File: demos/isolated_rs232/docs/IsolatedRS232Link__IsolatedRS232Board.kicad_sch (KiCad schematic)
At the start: 9 parts, among them J1 Header1xNFemale, J2 Header1xNFemale

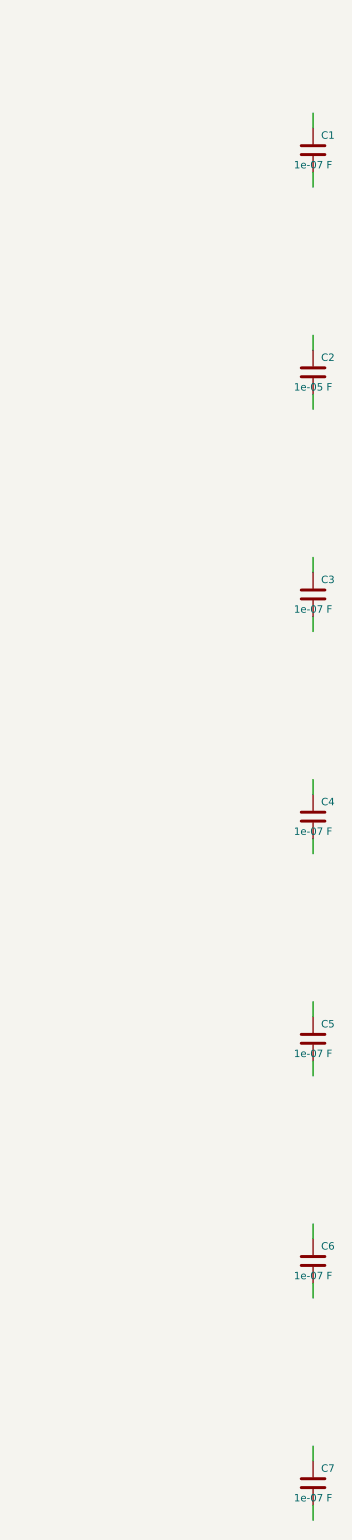
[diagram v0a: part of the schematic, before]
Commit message: framework: passive + diode terminals mandatory (#30)
Continuation of the LED.cathode regression fix (#29). Resistor,
Capacitor, Inductor, and every Diode subclass had their terminals
declared `mandatory=False` with the same "structurally inert under
graph evaluation" justification — letting demos declare BOM-only
timing / decoupling / pull-up parts without wiring them, then ship
breadboard SVGs and netlists where those parts sat orphaned.

A real resistor / capacitor / inductor / diode with a dangling
terminal does nothing. Marking the ports mandatory closes the
silent regression at the framework layer.

  - `src/components/passives/{resistor,capacitor,inductor}.py` and
    every diode subclass under `src/components/diodes/` now declare
    their terminals `mandatory=True`.
  - `tests/components/test_{resistor,capacitor,inductor}.py`:
    regression tests pin the new contract per component.
  - `tests/components/test_diode_mandatory_terminals.py` (new):
    parametrized over D1N4001 / D1N4007 / D1N4148 / D1N4728A /
    D1N4733A / D1N4742A / D1N5817.
  - Six demos (`backup_power`, `bldc_motor`, `dice`,
    `doorbell_protector`, `fan_cooling`, `isolated_rs232`) had
    declared-but-unwired passives — each now wires them either to
    their datasheet-correct net (e.g. DoorbellProtector's flyback
    diode anode joins the relay coil_minus net) or as an isolated
    0-Ω passthrough with `dynamically_driven=True` where the part
    is genuinely BOM-only and the voltage-only simulator can't
    honour its behaviour. Comments at each call site explain
    which kind.
  - Test fixtures across CLI, refdes, format-roundtrip, kicad
    import, and per-format renderer tests updated so they still
    pin down the specific error each one exists to catch without
    tripping the new mandatory-pin check first.
  - All demo docs regenerated; goldens refreshed.

After this commit the breadboard SVGs show every BOM part connected
to something — no more orphaned caps and resistors float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
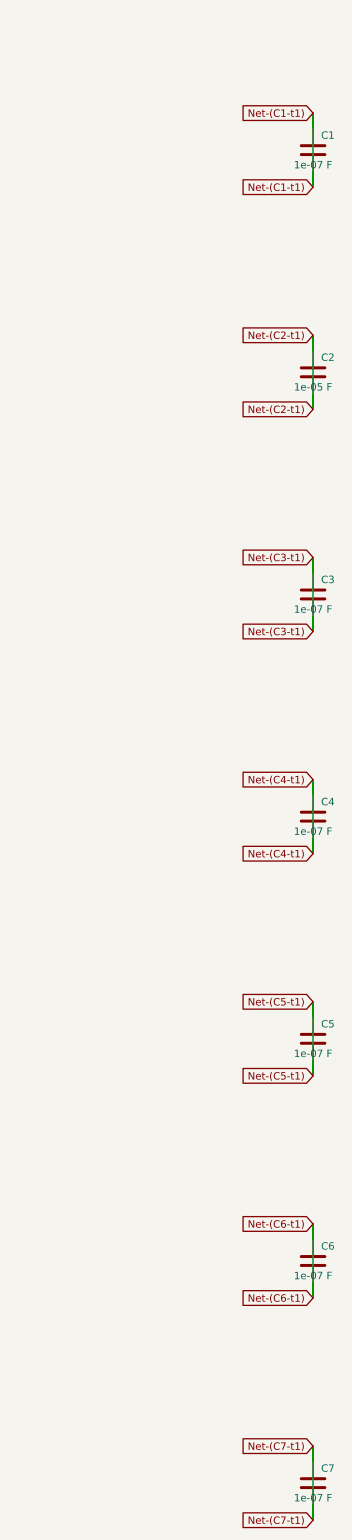
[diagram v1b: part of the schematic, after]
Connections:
- net Net-(C2-t1): now reaches C2.1
- net Net-(C2-t1): now also C2.2
- net Net-(C7-t1): now reaches C7.1
- net Net-(C7-t1): now also C7.2
- net Net-(C3-t1): now reaches C3.1
- net Net-(C3-t1): now also C3.2
- net Net-(C4-t1): now reaches C4.1
- net Net-(C4-t1): now also C4.2
- net Net-(C1-t1): now reaches C1.1
- net Net-(C1-t1): now also C1.2
- net Net-(C5-t1): now reaches C5.1
- net Net-(C5-t1): now also C5.2
- net Net-(C6-t1): now reaches C6.1
- net Net-(C6-t1): now also C6.2
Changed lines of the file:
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@@
     (stroke (width 0) (type default))
+  )
+  (global_label "Net-(C1-t1)"
+    (shape input)
+    (at 63.5 184.15 0)
+    (fields_autoplaced yes)
+    (effects (font (size 1.27 1.27)) (justify right))
+    (property "Intersheet References" "${INTERSHEET_REFS}"
+      (at 0 0 0)
+      (effects (font (size 1.27 1.27)) (hide yes))
+    )
   )
   (wire
     (pts (xy 63.5 173.99) (xy 63.5 171.45))
     (stroke (width 0) (type default))
+  )
+  (global_label "Net-(C1-t1)"
+    (shape input)
+    (at 63.5 171.45 0)
+    (fields_autoplaced yes)
+    (effects (font (size 1.27 1.27)) (justify right))
+    (property "Intersheet References" "${INTERSHEET_REFS}"
+      (at 0 0 0)
+      (effects (font (size 1.27 1.27)) (hide yes))
+    )
   )
   (symbol
@@
     (stroke (width 0) (type default))
   )
+  (global_label "Net-(C2-t1)"
+    (shape input)
+    (at 63.5 222.25 0)
+    (fields_autoplaced yes)
+    (effects (font (size 1.27 1.27)) (justify right))
+    (property "Intersheet References" "${INTERSHEET_REFS}"
+      (at 0 0 0)
+      (effects (font (size 1.27 1.27)) (hide yes))
+    )
+  )
   (wire
     (pts (xy 63.5 212.09) (xy 63.5 209.55))
     (stroke (width 0) (type default))
+  )
+  (global_label "Net-(C2-t1)"
+    (shape input)
+    (at 63.5 209.55 0)
+    (fields_autoplaced yes)
+    (effects (font (size 1.27 1.27)) (justify right))
+    (property "Intersheet References" "${INTERSHEET_REFS}"
+      (at 0 0 0)
+      (effects (font (size 1.27 1.27)) (hide yes))
+    )
   )
   (symbol
@@
     (stroke (width 0) (type default))
   )
+  (global_label "Net-(C3-t1)"
+    (shape input)
+    (at 63.5 260.35 0)
+    (fields_autoplaced yes)
+    (effects (font (size 1.27 1.27)) (justify right))
+    (property "Intersheet References" "${INTERSHEET_REFS}"
+      (at 0 0 0)
+      (effects (font (size 1.27 1.27)) (hide yes))
+    )
+  )
   (wire
     (pts (xy 63.5 250.19) (xy 63.5 247.65))
     (stroke (width 0) (type default))
+  )
+  (global_label "Net-(C3-t1)"
+    (shape input)
+    (at 63.5 247.65 0)
+    (fields_autoplaced yes)
+    (effects (font (size 1.27 1.27)) (justify right))
+    (property "Intersheet References" "${INTERSHEET_REFS}"
+      (at 0 0 0)
+      (effects (font (size 1.27 1.27)) (hide yes))
+    )
   )
   (symbol
@@
     (stroke (width 0) (type default))
   )
+  (global_label "Net-(C4-t1)"
+    (shape input)
+    (at 63.5 298.45 0)
+    (fields_autoplaced yes)
+    (effects (font (size 1.27 1.27)) (justify right))
+    (property "Intersheet References" "${INTERSHEET_REFS}"
+      (at 0 0 0)
+      (effects (font (size 1.27 1.27)) (hide yes))
+    )
+  )
   (wire
     (pts (xy 63.5 288.29) (xy 63.5 285.75))
     (stroke (width 0) (type default))
+  )
+  (global_label "Net-(C4-t1)"
+    (shape input)
+    (at 63.5 285.75 0)
+    (fields_autoplaced yes)
+    (effects (font (size 1.27 1.27)) (justify right))
+    (property "Intersheet References" "${INTERSHEET_REFS}"
+      (at 0 0 0)
+      (effects (font (size 1.27 1.27)) (hide yes))
+    )
   )
   (symbol
@@
     (stroke (width 0) (type default))
   )
+  (global_label "Net-(C5-t1)"
+    (shape input)
+    (at 63.5 336.55 0)
+    (fields_autoplaced yes)
+    (effects (font (size 1.27 1.27)) (justify right))
+    (property "Intersheet References" "${INTERSHEET_REFS}"
+      (at 0 0 0)
+      (effects (font (size 1.27 1.27)) (hide yes))
+    )
+  )
   (wire
     (pts (xy 63.5 326.39) (xy 63.5 323.85))
     (stroke (width 0) (type default))
+  )
+  (global_label "Net-(C5-t1)"
+    (shape input)
+    (at 63.5 323.85 0)
+    (fields_autoplaced yes)
+    (effects (font (size 1.27 1.27)) (justify right))
+    (property "Intersheet References" "${INTERSHEET_REFS}"
+      (at 0 0 0)
+      (effects (font (size 1.27 1.27)) (hide yes))
+    )
   )
   (symbol
@@
     (stroke (width 0) (type default))
   )
+  (global_label "Net-(C6-t1)"
+    (shape input)
+    (at 63.5 374.65 0)
+    (fields_autoplaced yes)
+    (effects (font (size 1.27 1.27)) (justify right))
+    (property "Intersheet References" "${INTERSHEET_REFS}"
+      (at 0 0 0)
+      (effects (font (size 1.27 1.27)) (hide yes))
+    )
+  )
   (wire
     (pts (xy 63.5 364.49) (xy 63.5 361.95))
     (stroke (width 0) (type default))
+  )
+  (global_label "Net-(C6-t1)"
+    (shape input)
+    (at 63.5 361.95 0)
+    (fields_autoplaced yes)
+    (effects (font (size 1.27 1.27)) (justify right))
+    (property "Intersheet References" "${INTERSHEET_REFS}"
+      (at 0 0 0)
+      (effects (font (size 1.27 1.27)) (hide yes))
+    )
   )
   (symbol
@@
     (stroke (width 0) (type default))
   )
+  (global_label "Net-(C7-t1)"
+    (shape input)
+    (at 63.5 412.75 0)
+    (fields_autoplaced yes)
+    (effects (font (size 1.27 1.27)) (justify right))
+    (property "Intersheet References" "${INTERSHEET_REFS}"
+      (at 0 0 0)
+      (effects (font (size 1.27 1.27)) (hide yes))
+    )
+  )
   (wire
     (pts (xy 63.5 402.59) (xy 63.5 400.05))
     (stroke (width 0) (type default))
+  )
+  (global_label "Net-(C7-t1)"
+    (shape input)
+    (at 63.5 400.05 0)
+    (fields_autoplaced yes)
+    (effects (font (size 1.27 1.27)) (justify right))
+    (property "Intersheet References" "${INTERSHEET_REFS}"
+      (at 0 0 0)
+      (effects (font (size 1.27 1.27)) (hide yes))
+    )
   )
   (symbol
@@
     (stroke (width 0) (type default))
   )
+  (wire
+    (pts (xy 63.5 171.45) (xy 63.5 184.15))
+    (stroke (width 0) (type default))
+  )
+  (wire
+    (pts (xy 63.5 209.55) (xy 63.5 222.25))
+    (stroke (width 0) (type default))
+  )
+  (wire
+    (pts (xy 63.5 247.65) (xy 63.5 260.35))
+    (stroke (width 0) (type default))
+  )
+  (wire
+    (pts (xy 63.5 285.75) (xy 63.5 298.45))
+    (stroke (width 0) (type default))
+  )
+  (wire
+    (pts (xy 63.5 323.85) (xy 63.5 336.55))
+    (stroke (width 0) (type default))
+  )
+  (wire
+    (pts (xy 63.5 361.95) (xy 63.5 374.65))
+    (stroke (width 0) (type default))
+  )
+  (wire
+    (pts (xy 63.5 400.05) (xy 63.5 412.75))
+    (stroke (width 0) (type default))
+  )

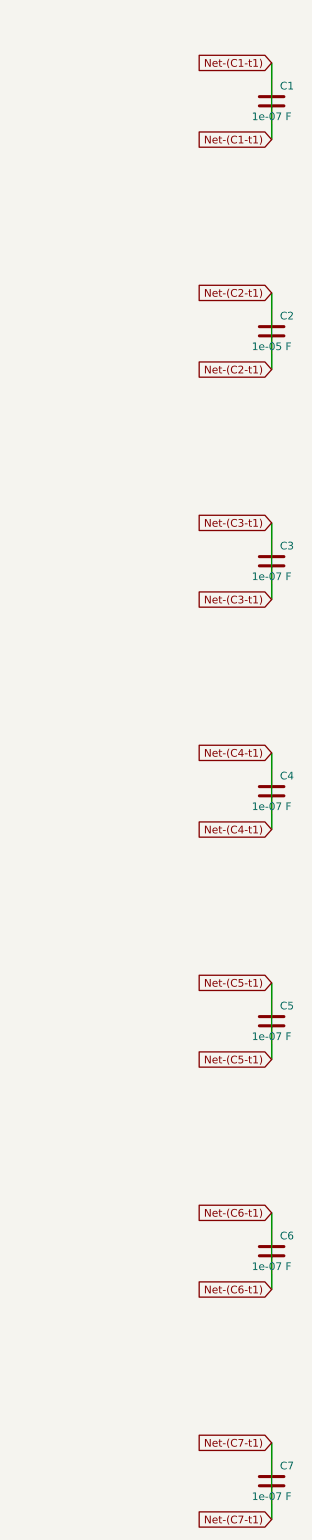
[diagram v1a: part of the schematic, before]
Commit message: units: Ohms.__str__ uses engineering notation (kΩ, MΩ, GΩ) (#33)
* units: Ohms.__str__ uses engineering notation (kΩ, MΩ, GΩ)

The previous `Ohms.__str__` formatted with bare `:.3g`, producing
unreadable scientific output for clean kilo / mega multiples:

  str(Ohms(10_000))     == "1e+04 Ω"      → now "10 kΩ"
  str(Ohms(100_000))    == "1e+05 Ω"      → now "100 kΩ"
  str(Ohms(1_000_000))  == "1e+06 Ω"      → now "1 MΩ"

The breadboard SVG visualiser surfaced the problem: a resistor body
labelled "100000Ω" makes a reader count zeros, while a label of
"100 kΩ" reads at a glance — exactly the convention every schematic
and parts catalogue uses. Centralising the engineering notation in
`Ohms.__str__` means every downstream consumer (assembly guide,
breadboard SVG, kicad netlist, BOM, reports) inherits the readable
form without each format adapter rolling its own formatter.

  - `Ohms.__str__` returns "47 Ω", "4.7 kΩ", "10 kΩ", "100 kΩ",
    "1 MΩ", "10 MΩ", "1 GΩ" per the kilo / mega / giga thresholds.
  - `Resistor.__str__` delegates to `str(self._ohms)` so it
    inherits the new notation (was producing the noisy "47.0 Ω"
    via raw float).
  - The breadboard visualiser's resistor body label uses
    `str(part.ohms)` directly (previously had a private
    `_format_ohms_compact` helper; removed).
  - `tests/components/test_resistor.py::test_str` updated for
    "47 Ω" (was "47.0 Ω"); new `test_str_renders_in_engineering_notation`
    pins kΩ / MΩ output across the kilo and mega thresholds.
  - All demo docs / goldens refreshed where the Ohms.__str__
    change affected the rendered output (breadboard SVGs, kicad
    sch value fields, BOM rows).

* units: Farads + Henries __str__ also use engineering notation

Same treatment as `Ohms.__str__` (previous commit) for the other two
passive engineering quantities. Demos contain caps and inductors
with values that the bare `:.3g` formatter would emit in scientific
form (`1e-07 F` for a 100 nF decoupling cap); centralising t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
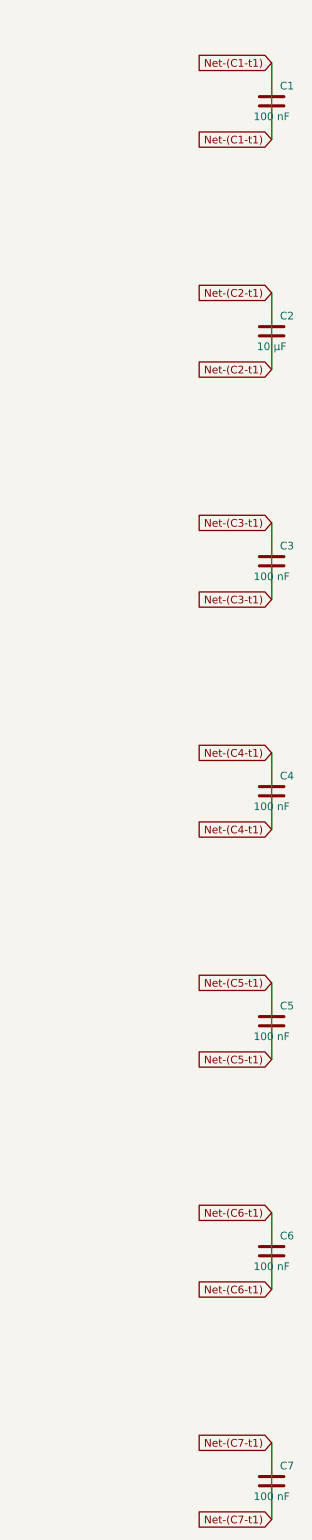
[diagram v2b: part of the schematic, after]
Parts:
- C1, C3, C4, C5, C6, C7: value 1e-07 F -> 100 nF
- C2: value 1e-05 F -> 10 µF
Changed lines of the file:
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@@
       (effects (font (size 1.27 1.27)))
     )
-    (property "Value" "1e-07 F"
+    (property "Value" "100 nF"
       (at 63.5 180.34 0)
       (effects (font (size 1.27 1.27)))
@@
       (effects (font (size 1.27 1.27)))
     )
-    (property "Value" "1e-05 F"
+    (property "Value" "10 µF"
       (at 63.5 218.44 0)
       (effects (font (size 1.27 1.27)))
@@
       (effects (font (size 1.27 1.27)))
     )
-    (property "Value" "1e-07 F"
+    (property "Value" "100 nF"
       (at 63.5 256.54 0)
       (effects (font (size 1.27 1.27)))
@@
       (effects (font (size 1.27 1.27)))
     )
-    (property "Value" "1e-07 F"
+    (property "Value" "100 nF"
       (at 63.5 294.64 0)
       (effects (font (size 1.27 1.27)))
@@
       (effects (font (size 1.27 1.27)))
     )
-    (property "Value" "1e-07 F"
+    (property "Value" "100 nF"
       (at 63.5 332.74 0)
       (effects (font (size 1.27 1.27)))
@@
       (effects (font (size 1.27 1.27)))
     )
-    (property "Value" "1e-07 F"
+    (property "Value" "100 nF"
       (at 63.5 370.84 0)
       (effects (font (size 1.27 1.27)))
@@
       (effects (font (size 1.27 1.27)))
     )
-    (property "Value" "1e-07 F"
+    (property "Value" "100 nF"
       (at 63.5 408.94 0)
       (effects (font (size 1.27 1.27)))
